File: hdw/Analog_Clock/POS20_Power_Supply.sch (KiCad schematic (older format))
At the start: 28 parts, among them Q601 FDC5612, U601 TLV6700, U602 LT3757

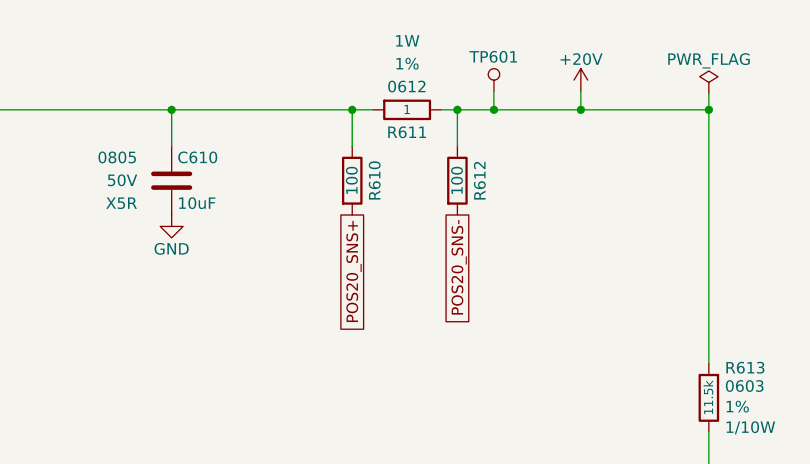
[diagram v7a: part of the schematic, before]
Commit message: Finished arranging parts, few netlist changes
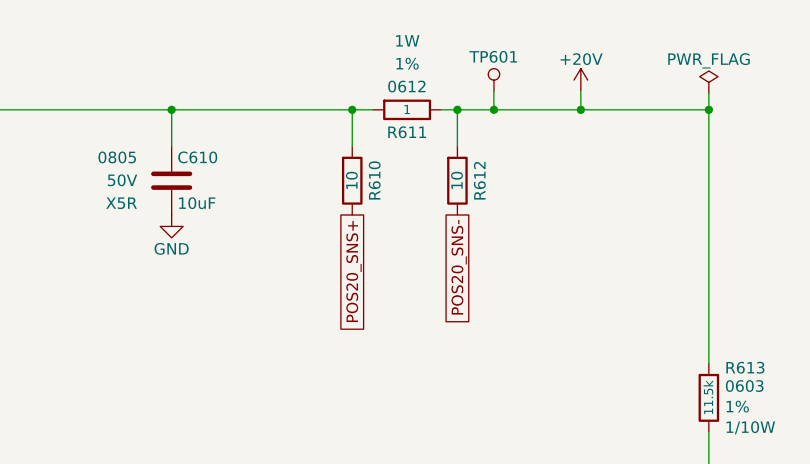
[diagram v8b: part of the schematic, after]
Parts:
- R610, R612: value 100 -> 10; Digi-Key PN RMCF0603FT100RCT-ND -> YAG2321CT-ND
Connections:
- net +20V: now also R612.1; no longer R612.2
- net POS20_SNS+: now also R610.2; no longer R610.1
- net POS20_SNS-: now also R612.2; no longer R612.1
- net at C610.1, D601.1 (K), R611.1: now also R610.1; no longer R610.2
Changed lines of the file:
@@
 	1    0    0    -1
-$EndComp
-$Comp
-L Custom_Library:R_Custom R?
-U 1 1 5E2D7420
-P 7750 1810
-AR Path="/5CB0BC26/5E2D7420" Ref="R?"  Part="1"
-AR Path="/5E1352F5/5E2D7420" Ref="R?"  Part="1"
-AR Path="/5CB6F1ED/5E2D7420" Ref="R?"  Part="1"
-AR Path="/5E0F9110/5E2D7420" Ref="R?"  Part="1"
-AR Path="/5A0BC776/5E2D7420" Ref="R?"  Part="1"
-AR Path="/5E939D51/5E2D7420" Ref="R610"  Part="1"
-F 0 "R610" V 7650 1810 50  0000 C CNN
-F 1 "100" V 7750 1810 50  0000 C CNN
-F 2 "Resistors_SMD:R_0603" H 7750 1810 50  0001 C CNN
-F 3 "" H 7750 1810 50  0001 C CNN
-F 4 "0603" V 7850 1810 50  0001 C CNN "display_footprint"
-F 5 "1%" V 7950 1810 50  0001 C CNN "Tolerance"
-F 6 "1/10W" V 8050 1810 50  0001 C CNN "Wattage"
-F 7 "RMCF0603FT100RCT-ND" H 8050 2210 60  0001 C CNN "Digi-Key PN"
-	1    7750 1810
-	-1   0    0    1
-$EndComp
-$Comp
-L Custom_Library:R_Custom R?
-U 1 1 5E2D742A
-P 8210 1810
-AR Path="/5CB0BC26/5E2D742A" Ref="R?"  Part="1"
-AR Path="/5E1352F5/5E2D742A" Ref="R?"  Part="1"
-AR Path="/5CB6F1ED/5E2D742A" Ref="R?"  Part="1"
-AR Path="/5E0F9110/5E2D742A" Ref="R?"  Part="1"
-AR Path="/5A0BC776/5E2D742A" Ref="R?"  Part="1"
-AR Path="/5E939D51/5E2D742A" Ref="R612"  Part="1"
-F 0 "R612" V 8110 1810 50  0000 C CNN
-F 1 "100" V 8210 1810 50  0000 C CNN
-F 2 "Resistors_SMD:R_0603" H 8210 1810 50  0001 C CNN
-F 3 "" H 8210 1810 50  0001 C CNN
-F 4 "0603" V 8310 1810 50  0001 C CNN "display_footprint"
-F 5 "1%" V 8410 1810 50  0001 C CNN "Tolerance"
-F 6 "1/10W" V 8510 1810 50  0001 C CNN "Wattage"
-F 7 "RMCF0603FT100RCT-ND" H 8510 2210 60  0001 C CNN "Digi-Key PN"
-	1    8210 1810
-	-1   0    0    1
 $EndComp
 Wire Wire Line
@@
 	1    0    0    -1
 $EndComp
+$Comp
+L Custom_Library:R_Custom R?
+U 1 1 5F689312
+P 7750 1810
+AR Path="/5CB0BC26/5F689312" Ref="R?"  Part="1"
+AR Path="/5E1352F5/5F689312" Ref="R?"  Part="1"
+AR Path="/5CB6F1ED/5F689312" Ref="R?"  Part="1"
+AR Path="/5CB7718D/5F689312" Ref="R?"  Part="1"
+AR Path="/5EAE2D8A/5F689312" Ref="R?"  Part="1"
+AR Path="/5E939D31/5F689312" Ref="R?"  Part="1"
+AR Path="/5E939CFF/5F689312" Ref="R?"  Part="1"
+AR Path="/5E939D51/5F689312" Ref="R610"  Part="1"
+F 0 "R610" V 7650 1810 50  0000 C CNN
+F 1 "10" V 7750 1810 50  0000 C CNN
+F 2 "Resistors_SMD:R_0603" H 7750 1810 50  0001 C CNN
+F 3 "" H 7750 1810 50  0001 C CNN
+F 4 "0603" V 7850 1810 50  0001 C CNN "display_footprint"
+F 5 "1%" V 7950 1810 50  0001 C CNN "Tolerance"
+F 6 "1/10W" V 8050 1810 50  0001 C CNN "Wattage"
+F 7 "YAG2321CT-ND" H 7750 1810 50  0001 C CNN "Digi-Key PN"
+	1    7750 1810
+	-1   0    0    -1
+$EndComp
+$Comp
+L Custom_Library:R_Custom R?
+U 1 1 5F68931C
+P 8210 1810
+AR Path="/5CB0BC26/5F68931C" Ref="R?"  Part="1"
+AR Path="/5E1352F5/5F68931C" Ref="R?"  Part="1"
+AR Path="/5CB6F1ED/5F68931C" Ref="R?"  Part="1"
+AR Path="/5CB7718D/5F68931C" Ref="R?"  Part="1"
+AR Path="/5EAE2D8A/5F68931C" Ref="R?"  Part="1"
+AR Path="/5E939D31/5F68931C" Ref="R?"  Part="1"
+AR Path="/5E939CFF/5F68931C" Ref="R?"  Part="1"
+AR Path="/5E939D51/5F68931C" Ref="R612"  Part="1"
+F 0 "R612" V 8110 1810 50  0000 C CNN
+F 1 "10" V 8210 1810 50  0000 C CNN
+F 2 "Resistors_SMD:R_0603" H 8210 1810 50  0001 C CNN
+F 3 "" H 8210 1810 50  0001 C CNN
+F 4 "0603" V 8310 1810 50  0001 C CNN "display_footprint"
+F 5 "1%" V 8410 1810 50  0001 C CNN "Tolerance"
+F 6 "1/10W" V 8510 1810 50  0001 C CNN "Wattage"
+F 7 "YAG2321CT-ND" H 8210 1810 50  0001 C CNN "Digi-Key PN"
+	1    8210 1810
+	-1   0    0    -1
+$EndComp
 $EndSCHEMATC
